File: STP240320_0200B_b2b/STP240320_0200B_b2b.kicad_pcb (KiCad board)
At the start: 2 copper layers, 6.1 x 11.2 mm, 2 parts, among them J1 Conn_02x08_Odd_Even

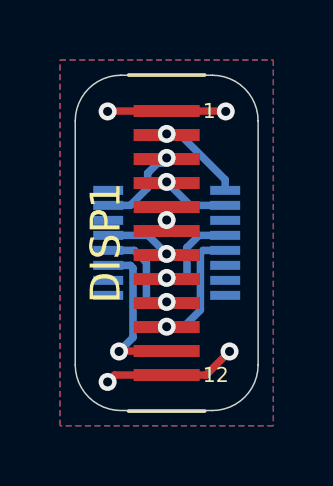
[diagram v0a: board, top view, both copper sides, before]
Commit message: Reverse board to board connector pinout.
Display symbol can now be used directly with 54722 parts.
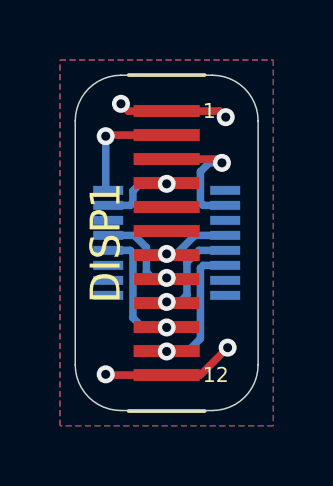
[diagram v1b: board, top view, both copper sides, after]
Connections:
- J1 pad 1: GND -> LEDK
- J1 pad 10: MOSI -> SCLK
- J1 pad 11: RESET -> GND
- J1 pad 12: GND -> RESET
- J1 pad 2: LEDK -> GND
- J1 pad 3: LEDA -> +3V3
- J1 pad 4: +3V3 -> LEDA
- J1 pad 7: DC -> CS
- J1 pad 8: CS -> DC
- J1 pad 9: SCLK -> MOSI
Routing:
- net LEDA: track 2.95 -> 4.63 mm
- net LEDK: track 2.98 -> 3.89 mm
- net RESET: track 5.43 -> 4.53 mm
- net GND: track 8.80 -> 8.13 mm, vias 5 -> 4
